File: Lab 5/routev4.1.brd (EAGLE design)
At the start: 100 x 80 mm, 48 parts, among them J1 FTDI_DEVICE, M1 WIRELESS-NRF24L01, U2 GY-521MPU6050, U3 ATMEGA328P_TQFP

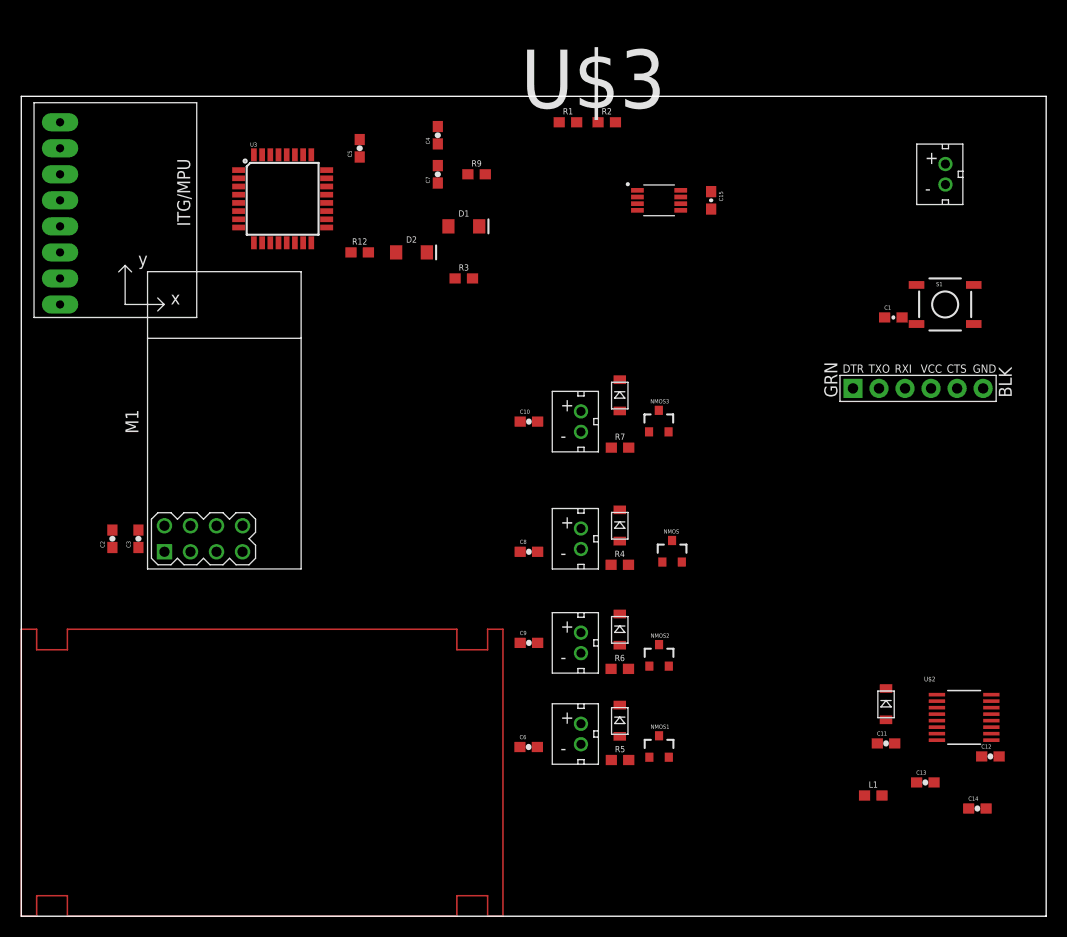
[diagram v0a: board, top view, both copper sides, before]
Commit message: routev4.1 idea crashed and burned: FTDI not the right module Ugggg; Update Template replacing with the correct one
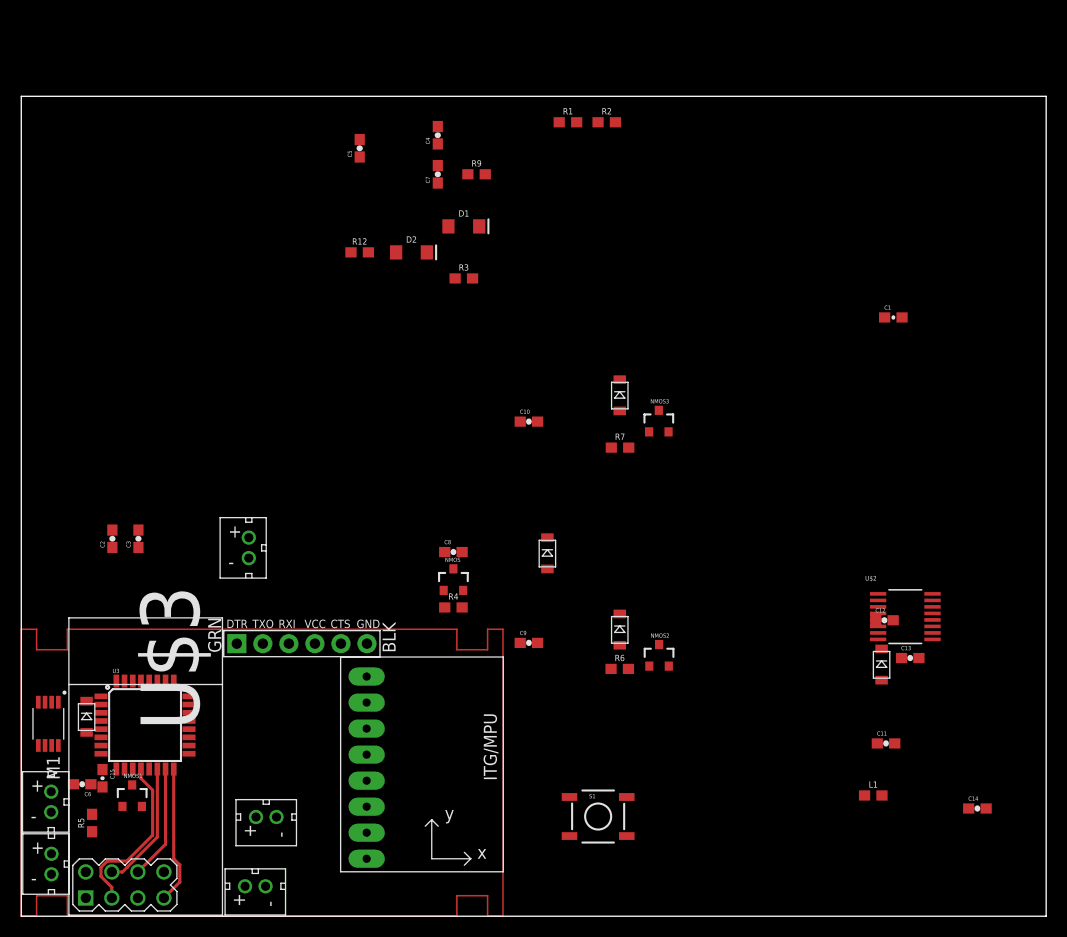
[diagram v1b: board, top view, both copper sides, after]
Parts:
- removed J1: FTDI_DEVICE, quad:FTDI_DEVICE_SIDE
- added J2: FTDI_DEVICE, quad:FTDI_DEVICE_SIDE
- moved C15 81.9 mm to (7.92, 13.5)
- moved U$3 78.5 mm to (2.64, 18.8), turned to 270 degrees
- moved U$1 77.1 mm to (22.2, 35.9)
- moved U2 61.8 mm to (42.6, 14.5)
- moved S1 60.4 mm to (56.3, 9.73)
- moved MOTOR2 56.0 mm to (2.95, 5.09)
- moved U3 53.1 mm to (12.1, 18.7)
- moved MOTOR1 52.1 mm to (2.92, 11.2)
- moved DIODE1 52.0 mm to (6.38, 19.4)
- moved R5 51.9 mm to (6.91, 9.09), turned to 90 degrees
- moved NMOS1 51.6 mm to (10.8, 11.7)
- moved MOTOR3 49.3 mm to (23.9, 9.68), turned to 90 degrees
- moved MOTOR 46.5 mm to (22.8, 2.92), turned to 90 degrees
- moved C6 43.7 mm to (5.94, 12.9), turned to 180 degrees
- moved M1 34.6 mm to (12.6, 14.5)
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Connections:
- net FTDI-RX: now also J2.P$3; no longer J1.P$3
- net FTDI-TX: now also J2.P$2; no longer J1.P$2
- net GND: now also J2.P$6; no longer J1.P$6
- net N$12: now also J2.P$1; no longer J1.P$1
- net VCC: now also J2.P$4; no longer J1.P$4
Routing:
- net RF-CE: track 0.00 -> 16.7 mm
- net RF-MISO: track 0.00 -> 13.5 mm
- net RF-CSN: track 0.00 -> 12.5 mm
- net RF-MOSI: track 0.00 -> 11.2 mm
